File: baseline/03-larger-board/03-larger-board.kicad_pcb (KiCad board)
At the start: 2 copper layers, 80.4 x 43.2 mm, 25 parts, among them J1 DB25MALE, J2 DB9MALE, P1 CONN_6, U1 74LS125, U2 74LS125

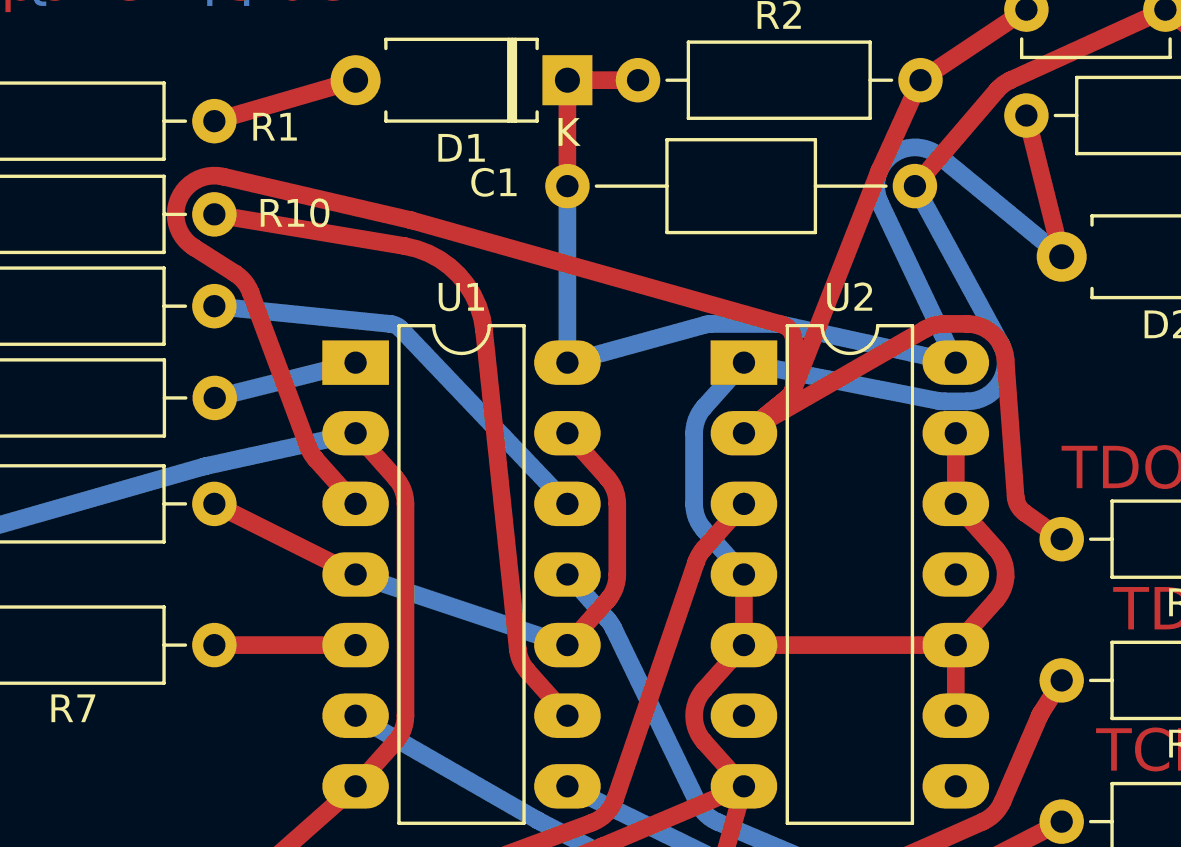
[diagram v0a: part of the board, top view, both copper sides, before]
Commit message: feat(bundle): route nets as a seated bundle rather than one after another
Sequential routing has a failure no ordering can fix. A gap wide enough
for two tracks: the first net through it is asked, alone, where a rubber
band would sit, and a rubber band sits in the middle. The second finds
the gap full. Re-routing the first puts it back exactly where it was --
the taut path is deterministic -- so ripping up and re-ordering only
swaps who is stranded.

Routing now happens in two stages. Every connection is first routed
against the static obstacles alone, which says which gap it *wants* --
including connections that a sequential pass would have blocked, so a
stranded net still gets a say. Gaps are then counted,
floor((D - c) / (w + c)) tracks each, contending nets are ordered across
each gap and given slots, and every connection is routed again against
obstacles inflated by its own slot's share. Nothing is pushed: each net
is simply handed a problem that already contains the others.

The slack in a gap has to be divided rather than handed to every net.
Giving each the full band let them all drift to the inside of it and end
up 1.5 apart where 2.0 was required; folding an equal share into the
stride fixes it, and any position in one band is then a full pitch from
any position in the next.

Slot assignment is a model, so the arrangement is verified afterwards on
real geometry and anything still too close is routed the old way. That
settling pass also reconsiders which layer a connection sits on --
choosing it before the contention is known left a two-layer board using
one layer and stranding a net on it.

Results are unchanged on all three boards, and that is the honest
finding rather than a disappointment to hide:

  ecc83-pp F.Cu        19/20 -> 19/20
  ecc83-pp F.Cu+B.Cu   20/20 -> 20/20
  sonde xilinx         63/66 -> 63/66, 0 DRC either way

The mechanism is proven on the case it exists for -- tests/test_bundle.py
shows the second net raising NoPathFound sequentiall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
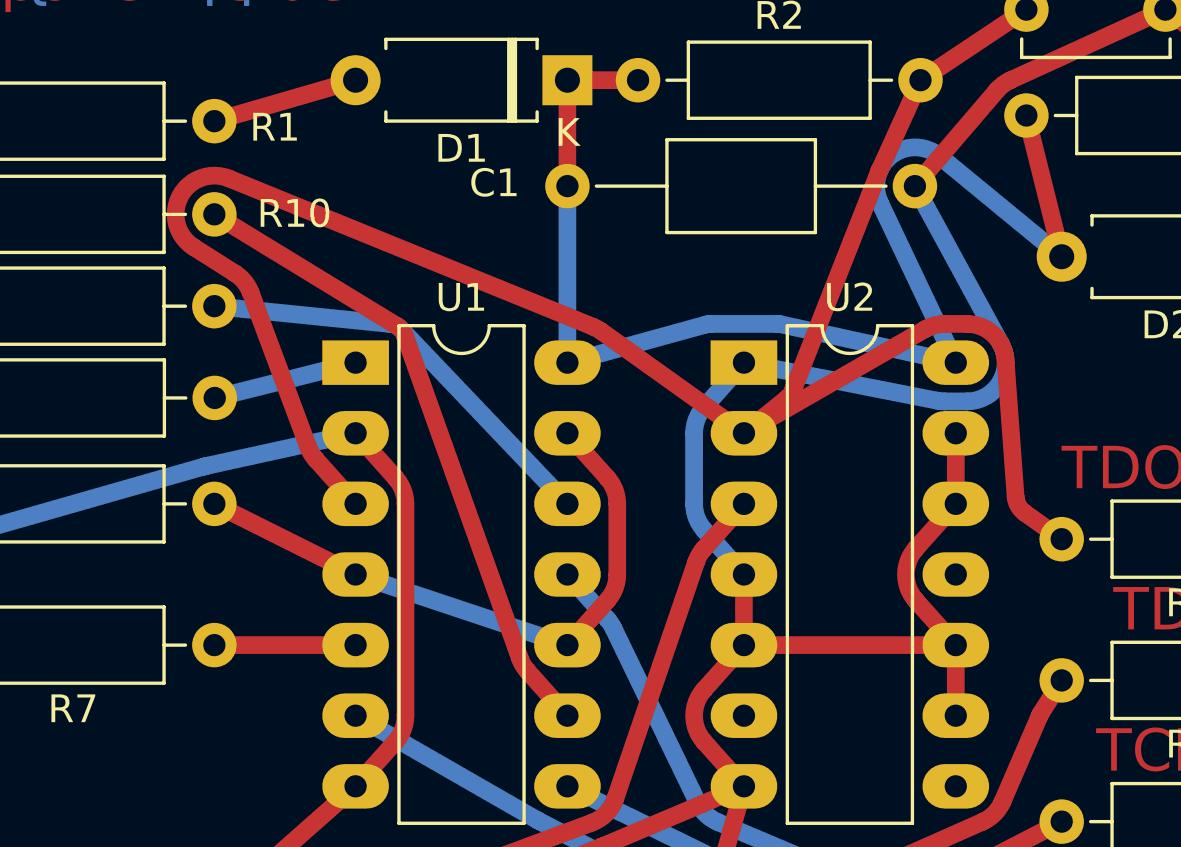
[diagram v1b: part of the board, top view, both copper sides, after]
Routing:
- net Net-(U1A-O): track 77.9 -> 73.2 mm
- net Net-(U1C-D): track 25.9 -> 23.2 mm
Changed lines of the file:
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@@
 	(segment
 		(start 121.92 77.216)
-		(end 128.765336 78.356335)
+		(end 128.509664 81.243314)
 		(width 0.635)
 		(layer "F.Cu")
@@
 	)
 	(arc
-		(start 128.765336 78.356335)
-		(mid 130.704312 79.390977)
-		(end 131.621361 81.388259)
+		(start 128.509664 81.243314)
+		(mid 128.660829 81.375488)
+		(end 128.7593 81.550485)
 		(width 0.635)
 		(layer "F.Cu")
@@
 	)
 	(segment
-		(start 131.621361 81.388259)
-		(end 132.833906 92.856552)
+		(start 128.7593 81.550485)
+		(end 132.907207 93.178303)
 		(width 0.635)
 		(layer "F.Cu")
@@
 	)
 	(arc
-		(start 132.833906 92.856552)
-		(mid 132.945741 93.274799)
+		(start 132.907207 93.178303)
+		(mid 133.021561 93.421672)
 		(end 133.180518 93.638554)
 		(width 0.635)
@@
 	(segment
 		(start 140.97 85.09)
-		(end 142.544437 83.810889)
-		(width 0.635)
-		(layer "F.Cu")
-		(net 16)
-	)
-	(arc
-		(start 142.544437 83.810889)
-		(mid 142.706177 83.605219)
-		(end 142.76382 83.35)
-		(width 0.635)
-		(layer "F.Cu")
-		(net 16)
-	)
-	(segment
-		(start 142.76382 83.35)
-		(end 142.76382 81.75)
-		(width 0.635)
-		(layer "F.Cu")
-		(net 16)
-	)
-	(arc
-		(start 142.76382 81.75)
-		(mid 142.643347 81.39144)
-		(end 142.330809 81.178368)
-		(width 0.635)
-		(layer "F.Cu")
-		(net 16)
-	)
-	(segment
-		(start 142.330809 81.178368)
-		(end 129.019677 77.433735)
-		(width 0.635)
-		(layer "F.Cu")
-		(net 16)
-	)
-	(segment
-		(start 129.019677 77.433735)
-		(end 128.9789 77.423273)
-		(width 0.635)
-		(layer "F.Cu")
-		(net 16)
-	)
-	(segment
-		(start 128.9789 77.423273)
-		(end 122.235086 75.858261)
-		(width 0.635)
-		(layer "F.Cu")
-		(net 16)
-	)
-	(arc
-		(start 122.235086 75.858261)
-		(mid 120.634504 76.677265)
+		(end 135.830561 81.416102)
+		(width 0.635)
+		(layer "F.Cu")
+		(net 16)
+	)
+	(arc
+		(start 135.830561 81.416102)
+		(mid 135.692691 81.329254)
+		(end 135.545627 81.259089)
+		(width 0.635)
+		(layer "F.Cu")
+		(net 16)
+	)
+	(segment
+		(start 135.545627 81.259089)
+		(end 122.445627 75.925089)
+		(width 0.635)
+		(layer "F.Cu")
+		(net 16)
+	)
+	(arc
+		(start 122.445627 75.925089)
+		(mid 120.681236 76.577096)
 		(end 121.172934 78.392702)
 		(width 0.635)
@@
 		(net 37)
 	)
-	(segment
+	(arc
 		(start 136.059482 91.098554)
-		(end 136.137135 91.003513)
-		(width 0.635)
-		(layer "F.Cu")
-		(net 37)
-	)
-	(arc
-		(start 136.137135 91.003513)
-		(mid 136.342841 90.609118)
+		(mid 136.322226 90.666933)
 		(end 136.41382 90.17)
 		(width 0.635)
@@
 	(segment
 		(start 148.59 92.71)
-		(end 150.029482 91.098554)
-		(width 0.635)
-		(layer "F.Cu")
-		(net 13)
-	)
-	(arc
-		(start 150.029482 91.098554)
-		(mid 150.273144 90.714312)
-		(end 150.380078 90.272069)
-		(width 0.635)
-		(layer "F.Cu")
-		(net 13)
-	)
-	(arc
-		(start 150.380078 90.272069)
-		(mid 150.309559 89.721114)
-		(end 150.029482 89.241446)
-		(width 0.635)
-		(layer "F.Cu")
-		(net 13)
-	)
-	(segment
-		(start 150.029482 89.241446)
+		(end 147.150518 91.098554)
+		(width 0.635)
+		(layer "F.Cu")
+		(net 13)
+	)
+	(arc
+		(start 147.150518 91.098554)
+		(mid 146.79618 90.17)
+		(end 147.150518 89.241446)
+		(width 0.635)
+		(layer "F.Cu")
+		(net 13)
+	)
+	(segment
+		(start 147.150518 89.241446)
 		(end 148.59 87.63)
 		(width 0.635)
